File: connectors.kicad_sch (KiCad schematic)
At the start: 4 parts, among them J1 0436500218, J2 0430450212, J3 0430451200, J4 0430451024

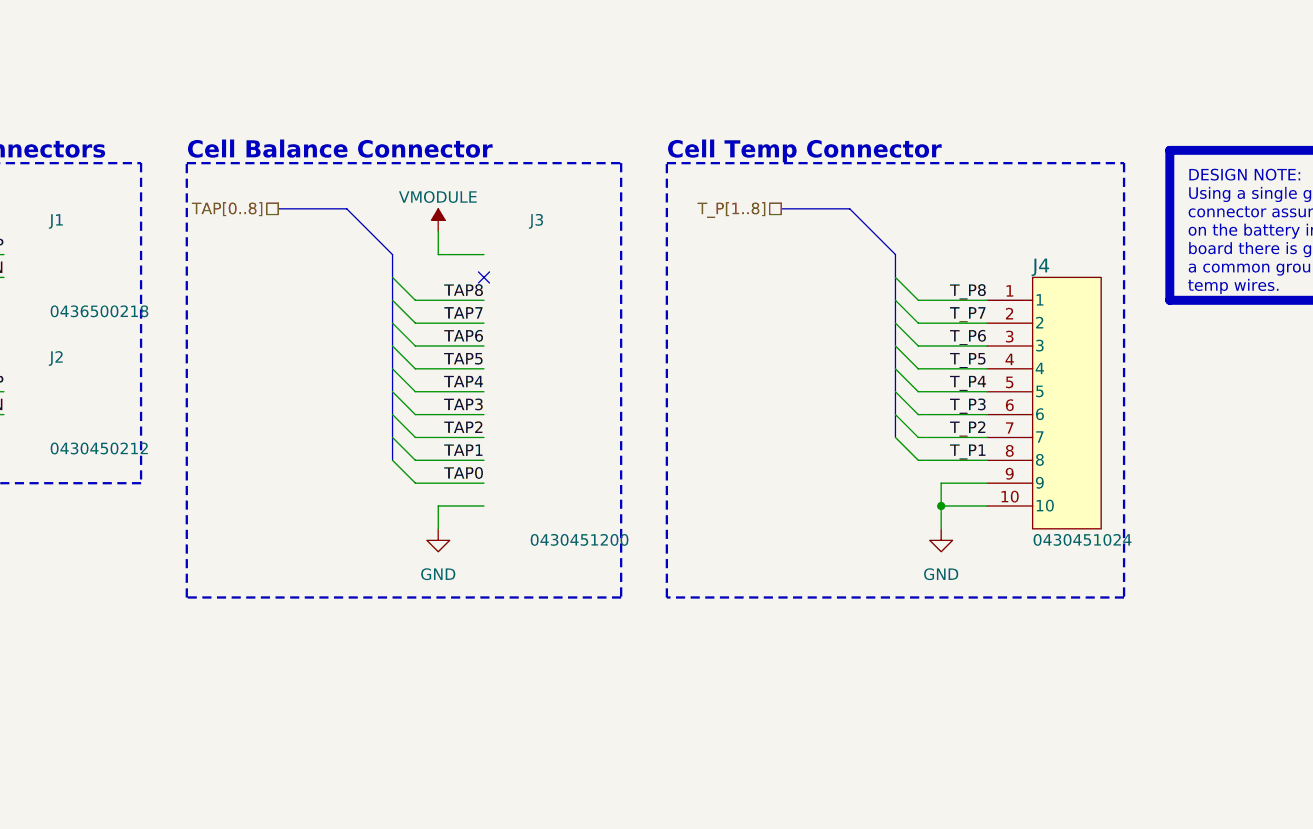
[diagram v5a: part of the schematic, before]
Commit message: PCB[Routing, Power, Connectors, Board Size]:Adjusted routing for temp and sens, placed bjt on board, adjusted connector placement and connections, changed board sized to match connectors better.
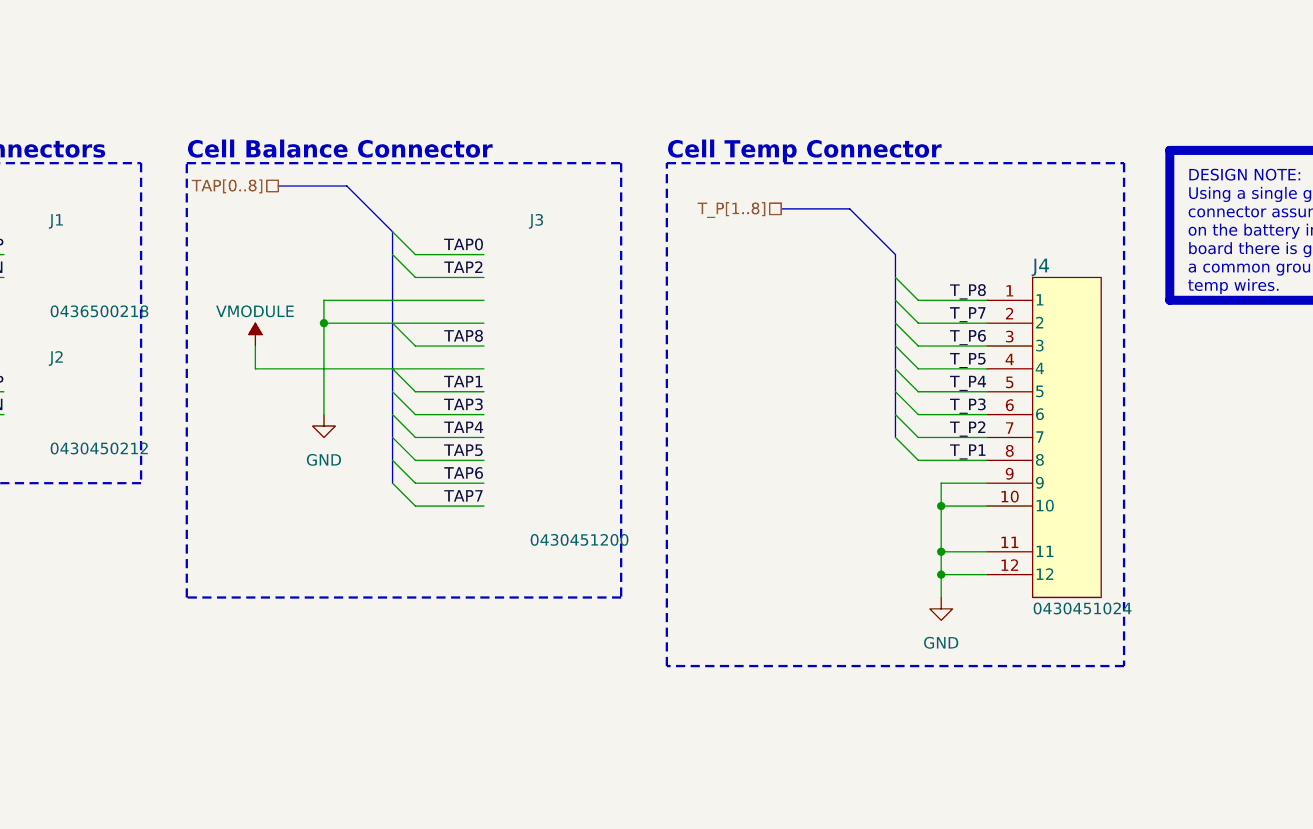
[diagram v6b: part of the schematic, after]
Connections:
- net GND: now also J3.3, J3.4, J4.11, J4.12; no longer J3.12
- net TAP0: now also J3.1; no longer J3.11
- net TAP1: now also J3.7; no longer J3.10
- net TAP2: now also J3.2; no longer J3.9
- net TAP4: now also J3.9; no longer J3.7
- net TAP5: now also J3.10; no longer J3.6
- net TAP6: now also J3.11; no longer J3.5
- net TAP7: now also J3.12; no longer J3.4
- net TAP8: now also J3.5; no longer J3.3
- net VMODULE: now also J3.6; no longer J3.1
- no-connect marks 1 -> 0

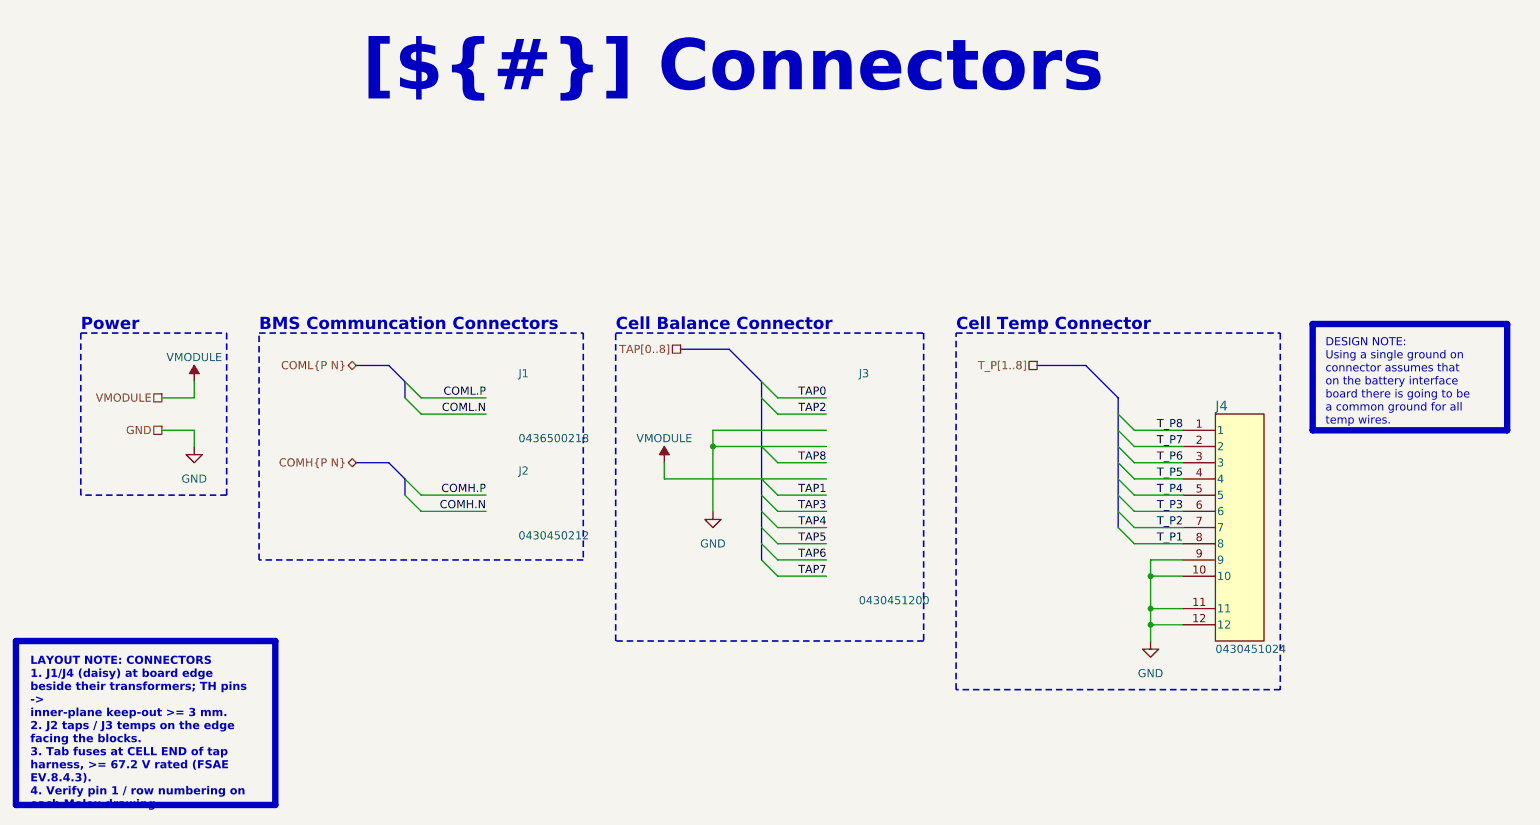
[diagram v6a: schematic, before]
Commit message: PCB[Layout]: Inital layout changes for board to board connector change. >> SCH[Connector]: Changed connectors for right angle micro fit 3.0 for iso spi chanels, and changed to board to board samtech for temp and tap.
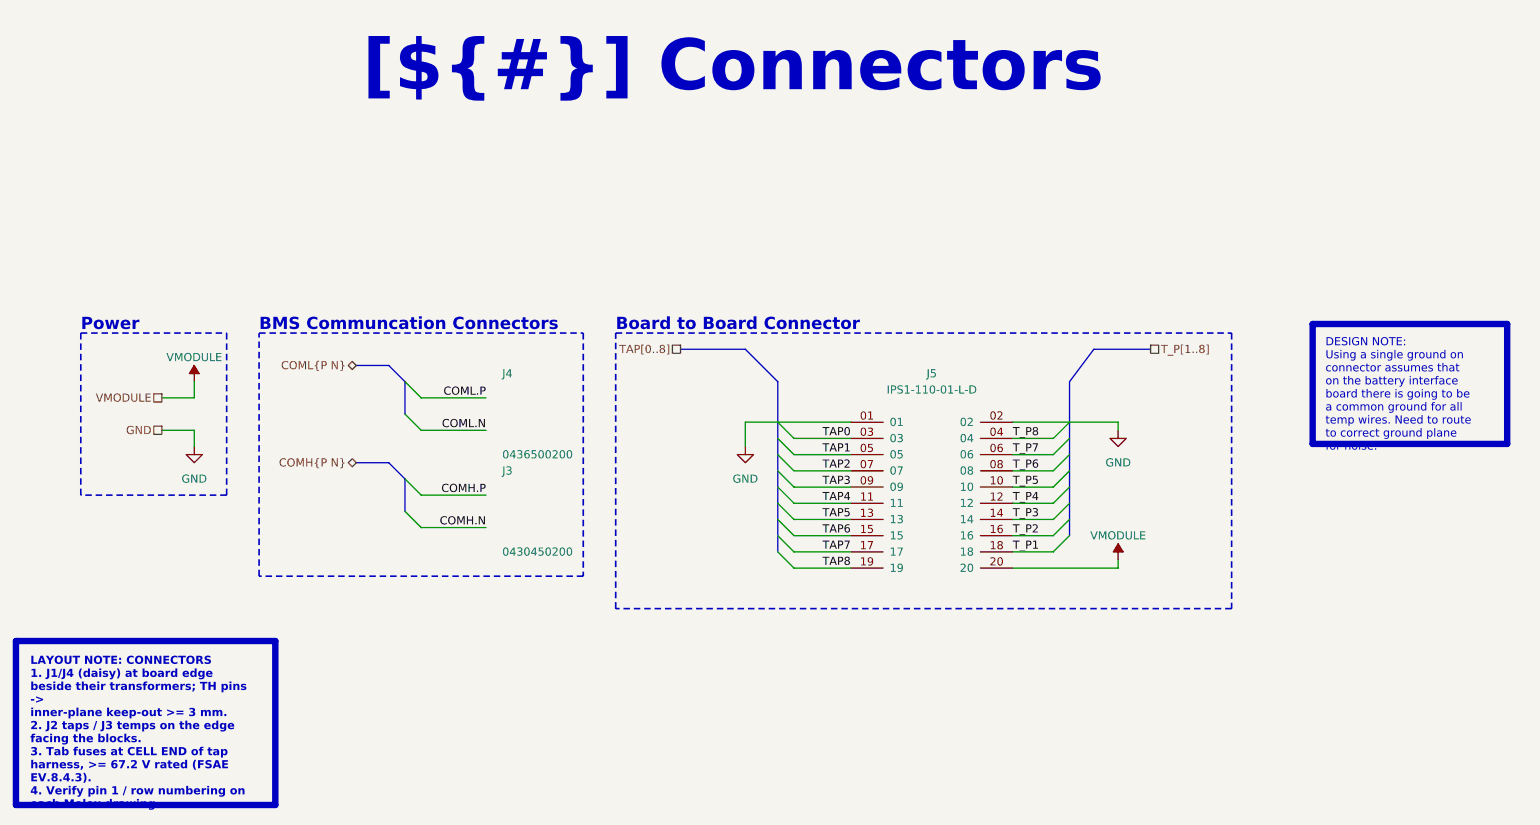
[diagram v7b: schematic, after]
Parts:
- removed J1: 0436500218, remote_0436500218:CONN_SD-43650-007_02_MOL, symbol remote_0436500218:0436500218
- removed J2: 0430450212, remote_0430450212:CONN_SD-43045-005_02_MOL, symbol remote_0430450212:0430450212
- removed J3: 0430451200, remote_0430451200:CONN_SD-43045-001_12_MOL, symbol remote_0430451200:0430451200
- removed J4: 0430451024, remote_0430451024:CONN_SD-43045-009_10_MOL, symbol remote_0430451024:0430451024
- added J3: 0430450200, remote_0430450200:CONN_SD-43045-001_02_MOL, symbol remote_0430450200:0430450200
- added J4: 0436500200, remote_0436500200:CONN_SD-43650-001_02_MOL, symbol remote_0436500200:0436500200
- added J5: IPS1-110-01-L-D, remote_ips1-110-01-l-d:SAMTEC_IPS1-110-01-L-D, symbol remote_ips1-110-01-l-d:IPS1-110-01-L-D
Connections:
- net COMH.N: now also J3.2
- net COMH.P: now also J3.1
- net COML.N: now also J4.2
- net COML.P: now also J4.1
- net GND: now also J5.01, J5.02
- net TAP0: now also J5.03
- net TAP1: now also J5.05
- net TAP2: now also J5.07
- net TAP3: now also J5.09
- net TAP4: now also J5.11
- net TAP5: now also J5.13
- net TAP6: now also J5.15
- net TAP7: now also J5.17
- net TAP8: now also J5.19
- net T_P1: now also J5.18
- net T_P2: now also J5.16
- net T_P3: now also J5.14
- net T_P4: now also J5.12
- net T_P5: now also J5.10
- net T_P6: now also J5.08
- net T_P7: now also J5.06
- net T_P8: now also J5.04
- net VMODULE: now also J5.20
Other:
- note added: "Board to Board Connector"
- note removed: "Cell Balance Connector"
- note removed: "Cell Temp Connector"

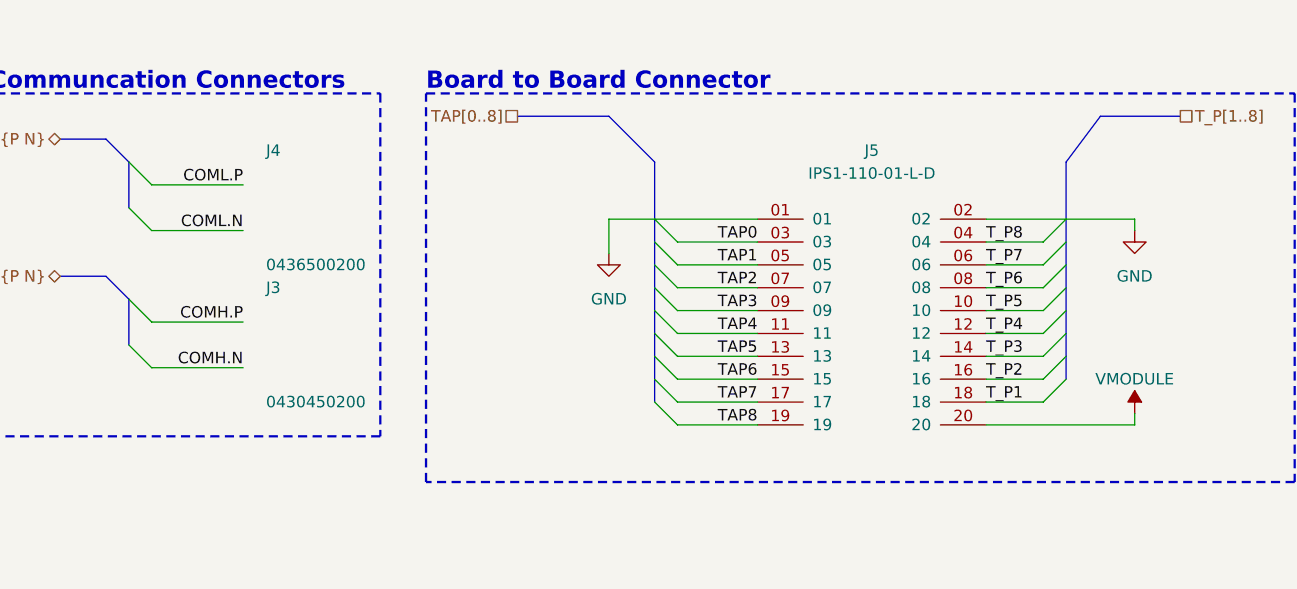
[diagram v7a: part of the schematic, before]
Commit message: PCB[Routing, Silk]: Everything but led routed, need to do via stiching, and finish adding silk screen.
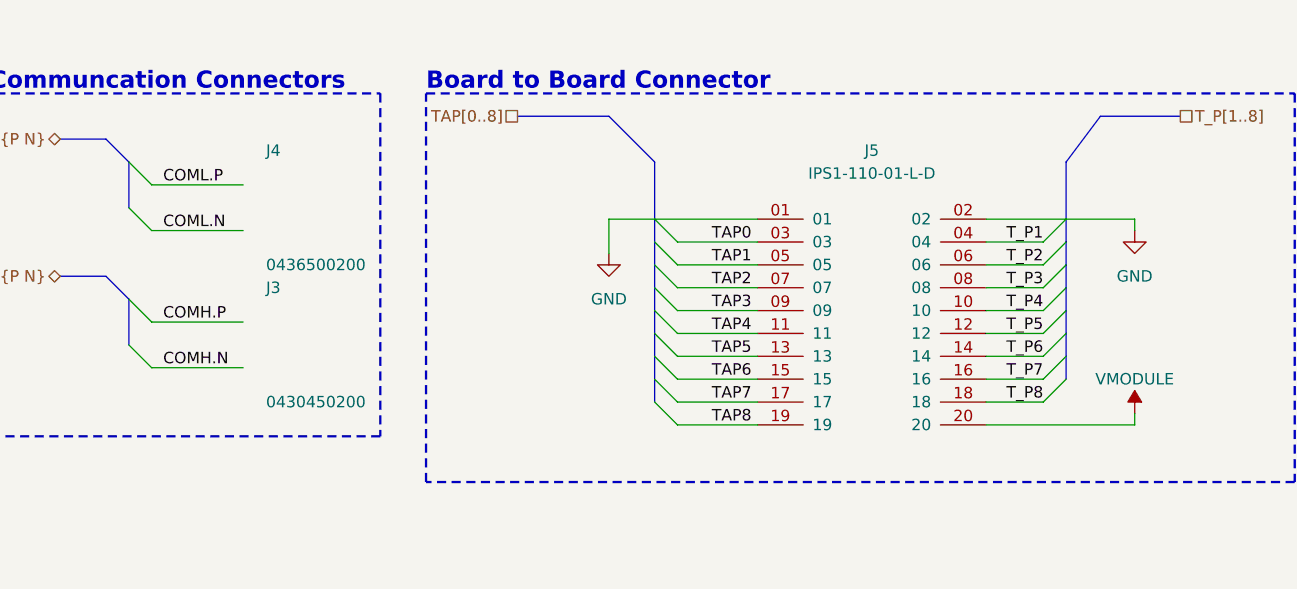
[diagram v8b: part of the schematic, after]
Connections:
- net COML.N: now also J4.1; no longer J4.2
- net COML.P: now also J4.2; no longer J4.1
- net T_P1: now also J5.04; no longer J5.18
- net T_P2: now also J5.06; no longer J5.16
- net T_P3: now also J5.08; no longer J5.14
- net T_P4: now also J5.10; no longer J5.12
- net T_P5: now also J5.12; no longer J5.10
- net T_P6: now also J5.14; no longer J5.08
- net T_P7: now also J5.16; no longer J5.06
- net T_P8: now also J5.18; no longer J5.04
